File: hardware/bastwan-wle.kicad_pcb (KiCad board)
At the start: 2 copper layers, 50.8 x 22.9 mm, 38 parts, among them J1 USB_C, J2 Conn_Right, J3 Conn_Left, J4 Conn_Battery, J5 SWD, Q1 DMG3415U-7, SW1 RST, U1 RAK3172, U2 MCP1700_DFN6, U3 CP2104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

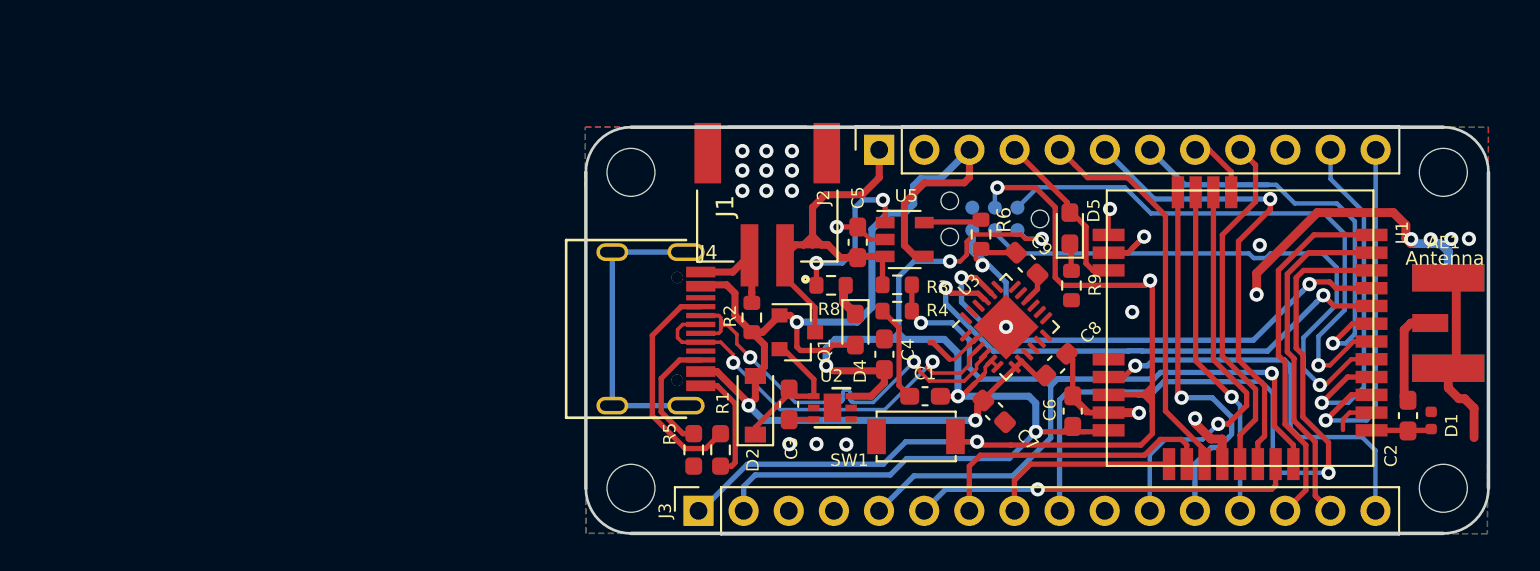
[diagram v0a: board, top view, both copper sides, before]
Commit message: Change_Footprint_RAK
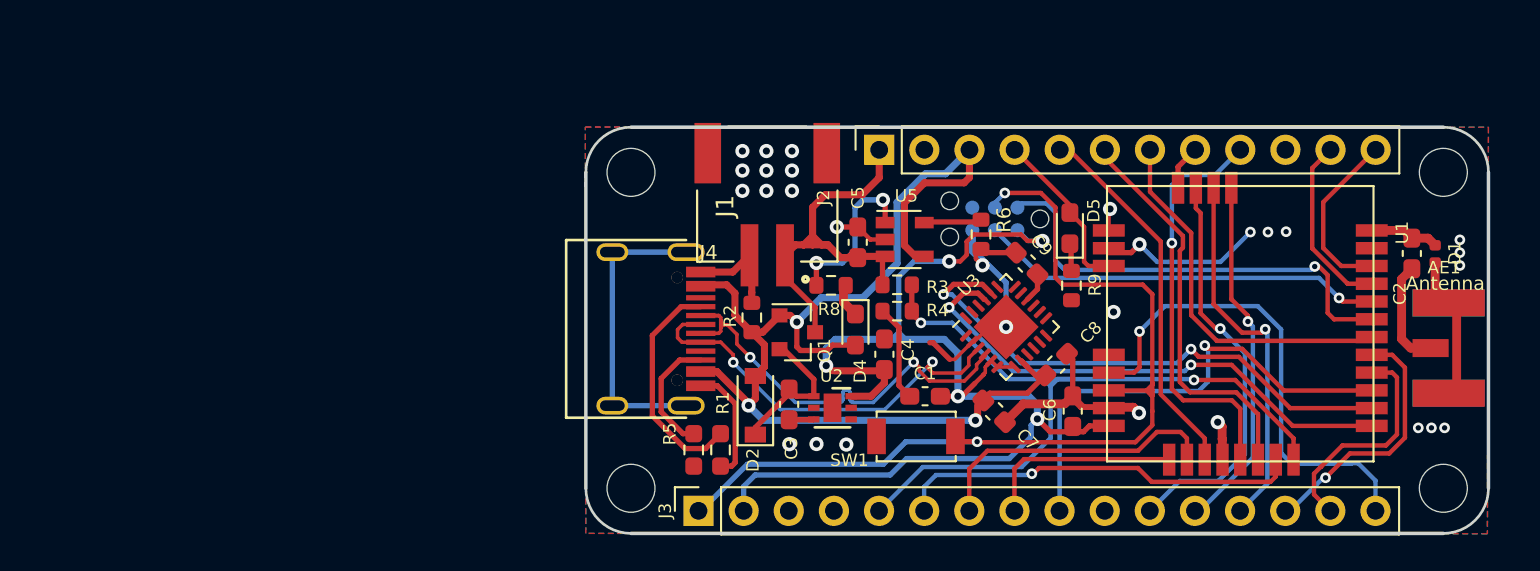
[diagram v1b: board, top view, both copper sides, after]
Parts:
- removed G***: LOGO, Aesthetics:bast_8x8
- C9: value 10uF -> 4.7uF
- moved D1 9.38 mm to (161.7, 69.8), turned to -90 degrees
- moved C2 9.13 mm to (160.4, 69.8), turned to -90 degrees
- moved AE1 1.41 mm to (164.5, 75.1)
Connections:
- J1 pad S1: Net-(J1-PadS1) -> unconnected-(J1-PadS1)
- J2 pad 2: Net-(J2-Pad2) -> unconnected-(J2-Pad2)
- J3 pad 10: Net-(J3-Pad10) -> unconnected-(J3-Pad10)
- J3 pad 3: Net-(J3-Pad3) -> unconnected-(J3-Pad3)
- J5 pad 6: Net-(J5-Pad6) -> unconnected-(J5-Pad6)
- U1 pad 1: /RX -> /TX_USB
- U1 pad 2: /TX -> /RX_USB
- U1 pad 4: /RX_USB -> /TX
- U1 pad 5: /TX_USB -> /RX
- U3 pad 1: Net-(U3-Pad1) -> unconnected-(U3-Pad1)
- U3 pad 10: Net-(U3-Pad10) -> unconnected-(U3-Pad10)
- U3 pad 11: Net-(U3-Pad11) -> unconnected-(U3-Pad11)
- U3 pad 12: Net-(U3-Pad12) -> unconnected-(U3-Pad12)
- U3 pad 13: Net-(U3-Pad13) -> unconnected-(U3-Pad13)
- U3 pad 14: Net-(U3-Pad14) -> unconnected-(U3-Pad14)
- U3 pad 15: Net-(U3-Pad15) -> unconnected-(U3-Pad15)
- U3 pad 17: Net-(U3-Pad17) -> unconnected-(U3-Pad17)
- U3 pad 18: Net-(U3-Pad18) -> unconnected-(U3-Pad18)
- U3 pad 19: Net-(U3-Pad19) -> unconnected-(U3-Pad19)
- U3 pad 22: Net-(U3-Pad22) -> unconnected-(U3-Pad22)
- U3 pad 23: Net-(U3-Pad23) -> unconnected-(U3-Pad23)
- U3 pad 24: Net-(U3-Pad24) -> unconnected-(U3-Pad24)
- U3 pad 7: VBUS -> +3V3
- U3 pad 9: Net-(U3-Pad9) -> unconnected-(U3-Pad9)
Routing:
- net unconnected-(J1-PadS1): track 0.00 -> 16.9 mm
- net Net-(J1-PadS1): track 16.9 -> 0.00 mm
- net /A4: track 42.4 -> 27.4 mm
- net /SDA: track 20.9 -> 9.90 mm, vias 1 -> 0
- net GND: track 83.0 -> 72.0 mm, vias 26 -> 29
- net /SCL: track 20.3 -> 10.1 mm, vias 1 -> 0
- net /SWCLK: track 31.7 -> 22.9 mm
- net /TX: track 19.6 -> 12.8 mm
- net /RX: track 20.7 -> 14.8 mm, vias 0 -> 1
- net /SWDIO: track 31.5 -> 25.7 mm
- net /BOOT0: track 23.0 -> 27.6 mm
- net /D11: track 26.9 -> 22.7 mm, vias 1 -> 0
- net /D6: track 20.0 -> 23.3 mm, vias 0 -> 1
- net /RST: track 56.7 -> 53.5 mm, vias 3 -> 2
- net /A0: track 46.7 -> 43.8 mm
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
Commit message: fix traces, update version v1.2
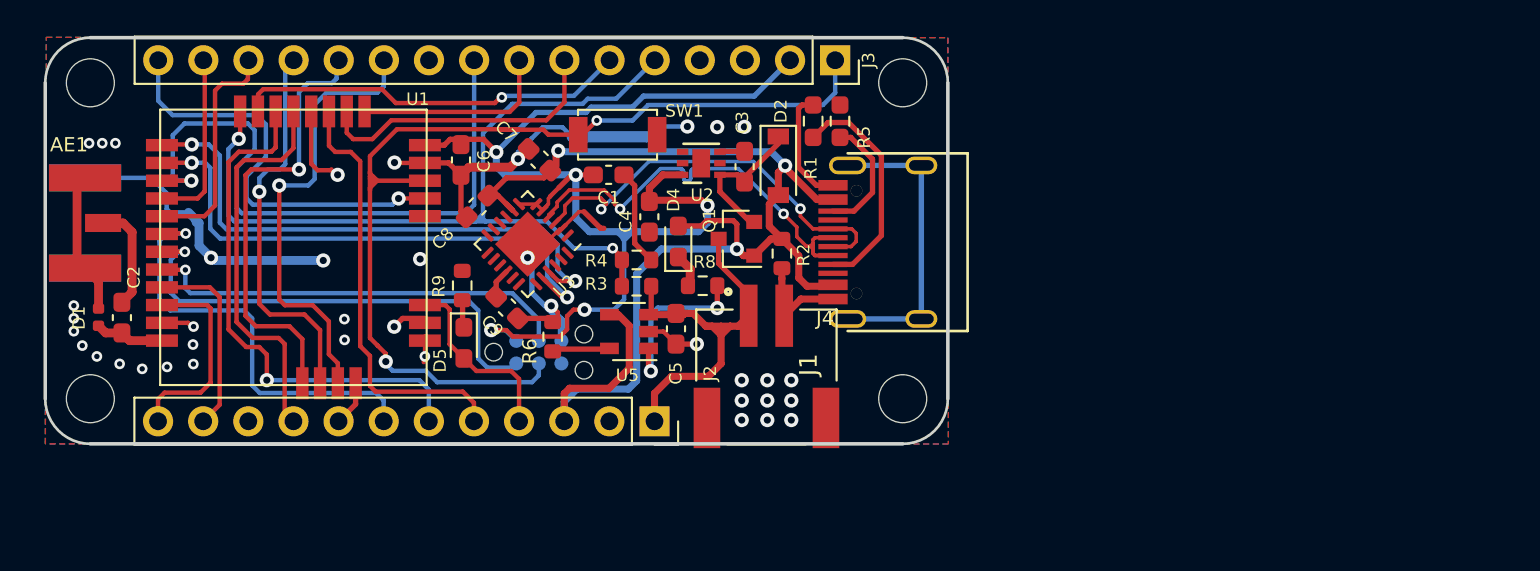
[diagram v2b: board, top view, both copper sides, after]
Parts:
- moved AE1 81.1 mm to (83.7, 68.0), turned to 0 degrees
- moved REF** 79.5 mm to (86.0, 60.2), turned to 180 degrees
- moved REF** 77.2 mm to (86.0, 77.9), turned to 180 degrees
- moved D1 75.3 mm to (86.5, 73.3), turned to 90 degrees
- moved C2 72.7 mm to (87.8, 73.4), turned to 90 degrees
- moved U1 69.1 mm to (90.0, 76.9), turned to 90 degrees
- moved C6 37.2 mm to (106.9, 64.5), turned to -90 degrees
- moved D5 34.7 mm to (107.0, 74.8), turned to -90 degrees
- moved R9 34.3 mm to (106.9, 71.6), turned to 90 degrees
- moved C8 33.8 mm to (107.8, 67.1), turned to -135 degrees
- moved SW1 29.8 mm to (112.9, 61.7), turned to 0 degrees
- moved C9 29.4 mm to (109.5, 72.8), turned to -45 degrees
- moved C7 29.2 mm to (111.3, 64.5), turned to 135 degrees
- moved REF** 27.5 mm to (131.7, 60.2), turned to 180 degrees
- moved U3 27.3 mm to (110.6, 69.2), turned to -135 degrees
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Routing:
- net GND: track 72.0 -> 96.3 mm, vias 29 -> 39
- net /A4: track 27.4 -> 36.7 mm
- net /D11: track 22.7 -> 29.7 mm, vias 0 -> 1
- net /COPI: track 20.2 -> 25.2 mm
- net /A0: track 43.8 -> 48.0 mm
- net /RST: track 53.5 -> 57.6 mm
- net /BOOT0: track 27.6 -> 23.8 mm
- net /D10: track 21.1 -> 24.7 mm, vias 0 -> 1
- net /D12: track 21.1 -> 24.2 mm
- net /TX: track 12.8 -> 9.99 mm
- net /CLK: track 23.0 -> 25.5 mm
- net VBUS: track 66.5 -> 68.7 mm
- net /TX_USB: track 29.3 -> 31.2 mm
- net /SDA: track 9.90 -> 11.6 mm
- net /RX: track 14.8 -> 13.2 mm, vias 1 -> 0
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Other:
- board text added: "v1.2"
- board text removed: "v1.1"

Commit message: Add labels and logo Bast
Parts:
- added G***: LOGO, Aesthetics:bast_8x8, B.Cu at (98.0, 67.5)
- added REF**: OSHW-Logo_7.5x8mm_SilkScreen, Symbol:OSHW-Logo_7.5x8mm_SilkScreen, B.Cu at (119.8, 70.0)
- added kibuzzard-61F04E1C: G***, kibuzzard-61F04E1C, F.Cu at (92.5, 60.7)
- added kibuzzard-61F04E1C: G***, kibuzzard-61F04E1C, B.Cu at (92.5, 60.6)
- added kibuzzard-61F04E29: G***, kibuzzard-61F04E29, F.Cu at (89.9, 60.7)
- added kibuzzard-61F04E29: G***, kibuzzard-61F04E29, B.Cu at (89.9, 60.5)
- added kibuzzard-61F04E3E: G***, kibuzzard-61F04E3E, F.Cu at (97.2, 60.6)
- added kibuzzard-61F04E3E: G***, kibuzzard-61F04E3E, B.Cu at (97.2, 60.5)
- added kibuzzard-61F04E50: G***, kibuzzard-61F04E50, F.Cu at (100.1, 60.6)
- added kibuzzard-61F04E50: G***, kibuzzard-61F04E50, B.Cu at (100.0, 60.5)
- added kibuzzard-61F04EE7: G***, kibuzzard-61F04EE7, F.Cu at (102.6, 60.6)
- added kibuzzard-61F04EE7: G***, kibuzzard-61F04EE7, B.Cu at (102.5, 60.5)
- added kibuzzard-61F04F06: G***, kibuzzard-61F04F06, F.Cu at (94.7, 60.6)
- added kibuzzard-61F04F06: G***, kibuzzard-61F04F06, B.Cu at (94.6, 60.5)
- added kibuzzard-61F04F1E: G***, kibuzzard-61F04F1E, F.Cu at (120.4, 60.8)
- added kibuzzard-61F04F1E: G***, kibuzzard-61F04F1E, B.Cu at (120.4, 60.8)
- added kibuzzard-61F04F3C: G***, kibuzzard-61F04F3C, F.Cu at (123.0, 60.7)
- added kibuzzard-61F04F3C: G***, kibuzzard-61F04F3C, F.Cu at (105.1, 60.7)
- added kibuzzard-61F04F3C: G***, kibuzzard-61F04F3C, F.Cu at (115.2, 77.3)
- added kibuzzard-61F04F3C: G***, kibuzzard-61F04F3C, B.Cu at (123.0, 60.8)
- added kibuzzard-61F04F3C: G***, kibuzzard-61F04F3C, B.Cu at (105.2, 60.5)
- added kibuzzard-61F04F3C: G***, kibuzzard-61F04F3C, B.Cu at (115.2, 77.4)
- added kibuzzard-61F04F78: G***, kibuzzard-61F04F78, F.Cu at (117.8, 60.7)
- added kibuzzard-61F04F78: G***, kibuzzard-61F04F78, B.Cu at (117.8, 60.7)
- added kibuzzard-61F04F8A: G***, kibuzzard-61F04F8A, F.Cu at (115.2, 60.7)
- added kibuzzard-61F04F8A: G***, kibuzzard-61F04F8A, B.Cu at (115.2, 60.6)
- added kibuzzard-61F04F96: G***, kibuzzard-61F04F96, F.Cu at (112.7, 60.7)
- added kibuzzard-61F04F96: G***, kibuzzard-61F04F96, B.Cu at (112.7, 60.6)
- added kibuzzard-61F04FA0: G***, kibuzzard-61F04FA0, F.Cu at (110.2, 60.7)
- added kibuzzard-61F04FA0: G***, kibuzzard-61F04FA0, B.Cu at (110.2, 60.6)
- added kibuzzard-61F04FAE: G***, kibuzzard-61F04FAE, F.Cu at (107.6, 60.7)
- added kibuzzard-61F04FAE: G***, kibuzzard-61F04FAE, B.Cu at (107.7, 60.7)
- added kibuzzard-61F04FBB: G***, kibuzzard-61F04FBB, F.Cu at (89.7, 77.4)
- added kibuzzard-61F04FBB: G***, kibuzzard-61F04FBB, B.Cu at (89.6, 77.4)
- added kibuzzard-61F04FC9: G***, kibuzzard-61F04FC9, F.Cu at (92.3, 77.4)
- added kibuzzard-61F04FC9: G***, kibuzzard-61F04FC9, B.Cu at (92.4, 77.4)
- added kibuzzard-61F04FDB: G***, kibuzzard-61F04FDB, F.Cu at (94.9, 77.4)
- added kibuzzard-61F04FDB: G***, kibuzzard-61F04FDB, B.Cu at (95.0, 77.4)
- added kibuzzard-61F04FE4: G***, kibuzzard-61F04FE4, F.Cu at (97.5, 77.5)
- added kibuzzard-61F04FE4: G***, kibuzzard-61F04FE4, B.Cu at (97.6, 77.4)
- added kibuzzard-61F04FF4: G***, kibuzzard-61F04FF4, F.Cu at (100.0, 77.4)
- added kibuzzard-61F04FF4: G***, kibuzzard-61F04FF4, B.Cu at (100.1, 77.4)
- added kibuzzard-61F0500D: G***, kibuzzard-61F0500D, F.Cu at (102.6, 77.4)
- added kibuzzard-61F0500D: G***, kibuzzard-61F0500D, B.Cu at (102.6, 77.4)
- added kibuzzard-61F050F3: G***, kibuzzard-61F050F3, F.Cu at (105.0, 77.3)
- added kibuzzard-61F050F3: G***, kibuzzard-61F050F3, B.Cu at (105.0, 77.4)
- added kibuzzard-61F050FC: G***, kibuzzard-61F050FC, F.Cu at (107.4, 77.4)
- added kibuzzard-61F050FC: G***, kibuzzard-61F050FC, B.Cu at (107.4, 77.5)
- added kibuzzard-61F05106: G***, kibuzzard-61F05106, F.Cu at (110.1, 77.4)
- added kibuzzard-61F05106: G***, kibuzzard-61F05106, B.Cu at (110.1, 77.4)
- added kibuzzard-61F05112: G***, kibuzzard-61F05112, F.Cu at (112.7, 77.4)
- added kibuzzard-61F05112: G***, kibuzzard-61F05112, B.Cu at (112.7, 77.4)
- added kibuzzard-61F051BF: G***, kibuzzard-61F051BF, F.Cu at (125.5, 60.7)
- added kibuzzard-61F051BF: G***, kibuzzard-61F051BF, B.Cu at (125.5, 60.7)
- added kibuzzard-61F051CB: G***, kibuzzard-61F051CB, F.Cu at (128.0, 60.7)
- added kibuzzard-61F051CB: G***, kibuzzard-61F051CB, B.Cu at (128.0, 60.7)
- added kibuzzard-61F0524D: G***, kibuzzard-61F0524D, F.Cu at (117.8, 77.3)
- added kibuzzard-61F0524D: G***, kibuzzard-61F0524D, B.Cu at (118.0, 77.4)
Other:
- board text removed: "3V3"
- board text removed: "A0"
- board text removed: "A1"
- board text removed: "A2"
- board text removed: "A3"
- board text removed: "A4"
- board text removed: "B0"
- board text removed: "CIPO"
- board text removed: "CLK"
- board text removed: "COPI"
- board text removed: "D10"
- board text removed: "D11"
- board text removed: "D12"
- board text removed: "D13"
- board text removed: "D5"
- board text removed: "D6"
- board text removed: "D9"
- board text removed: "EN"
- board text removed: "GND"
- board text removed: "NC"
- board text removed: "RX"
- board text removed: "SCL"
- board text removed: "SDA"
- board text removed: "TX"
- board text removed: "VBAT"
- board text removed: "VUSB"
- board text removed: "~{RST}"

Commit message: fix Ground
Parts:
- moved AE1 0.23 mm to (83.5, 68.0)
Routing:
- net GND: track 96.3 -> 88.2 mm

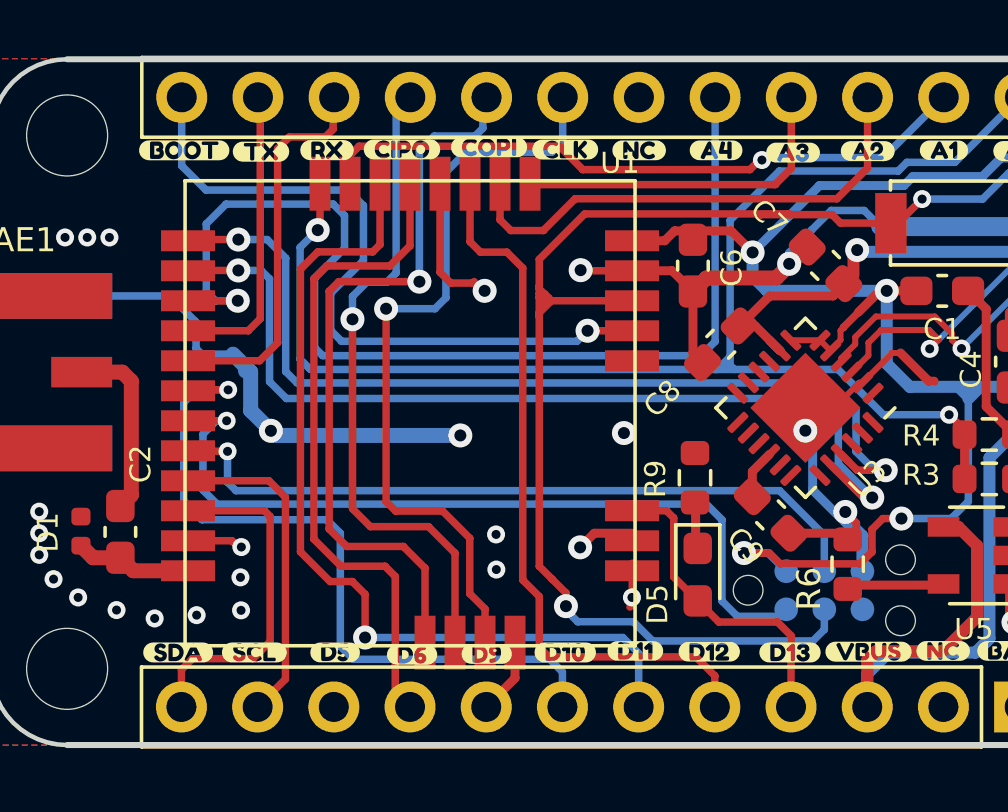
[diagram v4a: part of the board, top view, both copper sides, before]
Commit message: Fix SWD connector
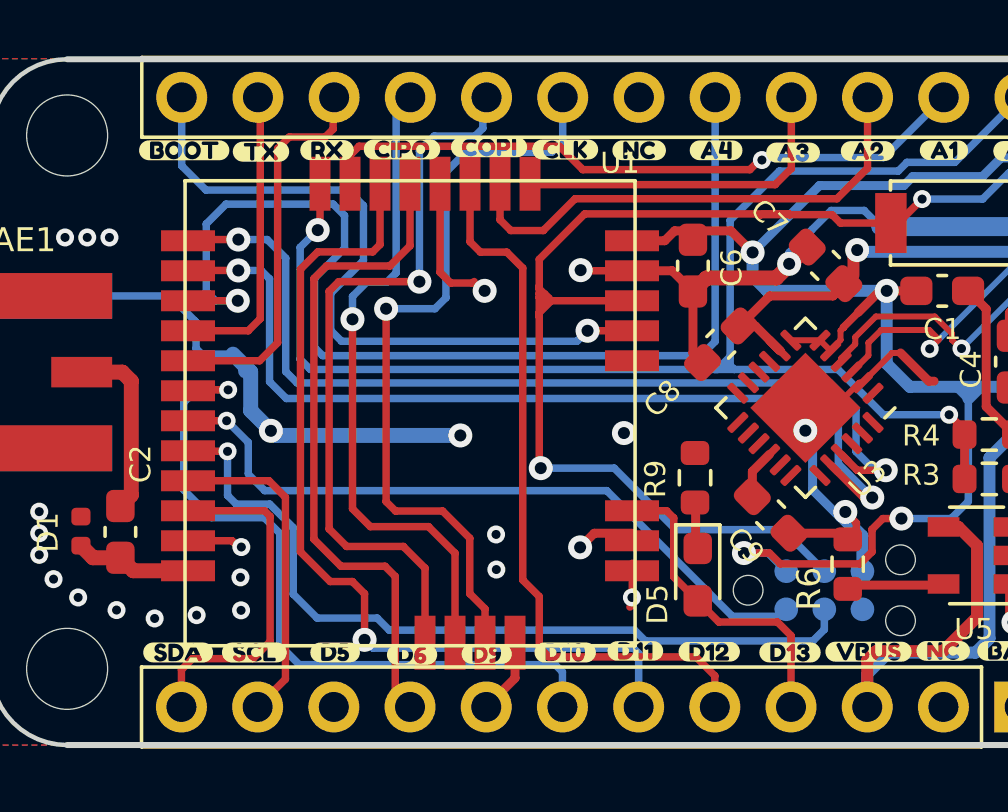
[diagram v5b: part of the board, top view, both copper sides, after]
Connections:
- J5 pad 3: /SWCLK -> /RST
- J5 pad 4: /RST -> /SWCLK
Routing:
- net /RST: track 57.6 -> 53.5 mm
- net /SWDIO: track 27.0 -> 23.3 mm
- net /SWCLK: track 24.2 -> 26.8 mm

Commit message: change label v1.3
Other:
- board text added: "v1.3"
- board text removed: "v1.2"
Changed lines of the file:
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@@
     (effects (font (size 1 1) (thickness 0.15)) (justify mirror))
   )
-  (gr_text "v1.2" (at 89.925 75.075) (layer "B.SilkS")
+  (gr_text "v1.3" (at 89.925 75.075) (layer "B.SilkS")
     (effects (font (size 1 1) (thickness 0.15)) (justify mirror))
   )
